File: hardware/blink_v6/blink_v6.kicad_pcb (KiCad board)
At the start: 2 copper layers, 130 x 70 mm, 241 parts, among them J1 RJ45, J12 Conn_01x06, J2 Conn_01x06_Pin, J3 Conn_01x05_Pin, J4 Conn_01x04_Pin, J5 Conn_01x06_Pin, J6 Conn_01x04_Pin, J7 Conn_01x04_Pin, J8 Conn_01x02, J9 Conn_02x10_Odd_Even, Q1 2N7002, Q10 2N7002, Q2 2N7002, Q3 2N7002, Q4 2N7002, Q5 2N7002, Q6 2N7002, Q7 2N7002, Q8 2N7002, Q9 2N7002, U1 ADA4807-1, U10 STM32F405RGTx, U11 AMS1117-3.3, U12 BA50DD0WHFP-TR, U13 M24C02-RMN, U2 SN74LVC1G14DBV, U3 SN74LVC1G14DBV, U4 ADA4807-1, U5 ADA4807-1, U6 TLV3603DCKR, U7 SN74LVC1G14DBV, U8 TLV3603DCKR, U9 L78L05_SOT89, X2 GTXO-14V (2.048MHz), Y1 AOCJY4A-10.000MHZ-SW, Y2 16MHz

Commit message: star clean up of blink board
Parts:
- removed ANT3, ANT4, ANT5, ANT6: U.FL-R-SMT-1, blinky_footprints:U.FL-R-SMT-1
- removed C1, C10, C17, C18, C2, C25, C26, C33, C45, C46, C48, C49: 100nF, Capacitor_SMD:C_0402_1005Metric
- removed C12, C14, C19, C23, C5, C7: 150pF, Capacitor_SMD:C_0603_1608Metric
- removed C13, C20, C8: 330pF, Capacitor_SMD:C_0603_1608Metric
- removed C15, C22, C6: 220pF, Capacitor_SMD:C_0603_1608Metric
- removed C16, C21, C3: 1nF, Capacitor_SMD:C_0603_1608Metric
- removed C24: 100nF, Capacitor_SMD:C_0603_1608Metric
- removed C34: 10uF, Capacitor_Tantalum_SMD:CP_EIA-3216-18_Kemet-A
- removed C42, C44: 33uF, Capacitor_Tantalum_SMD:CP_EIA-3528-21_Kemet-B
- removed J1: RJ45, Connector_RJ:RJ45_Amphenol_RJHSE5380
- removed J2: Conn_01x06_Pin, Connector_PinHeader_2.54mm:PinHeader_1x06_P2.54mm_Vertical
- removed J3: Conn_01x05_Pin, Connector_PinHeader_2.54mm:PinHeader_1x05_P2.54mm_Vertical
- removed JP1: SolderJumper_2_Bridged, Jumper:SolderJumper-2_P1.3mm_Bridged_RoundedPad1.0x1.5mm
- removed L1, L2, L3, L4, L5, L6: 1uF, Inductor_SMD:L_0805_2012Metric
- removed R1, R15, R16: 100R, Resistor_SMD:R_0603_1608Metric
- removed R10, R2, R6: 510R, Resistor_SMD:R_0603_1608Metric
- removed R11, R3, R7: 49R9, Resistor_SMD:R_0603_1608Metric
- removed R12, R13: 1K5, Resistor_SMD:R_0805_2012Metric
- removed R14: 330R, Resistor_SMD:R_0805_2012Metric
- removed R17: 20R, Resistor_SMD:R_0805_2012Metric
- removed R18, R21: 130K, Resistor_SMD:R_0603_1608Metric
- removed R19, R20, R22, R24, R60, R61: 1K0, Resistor_SMD:R_0603_1608Metric
- removed R23: 22K, Resistor_SMD:R_0805_2012Metric
- removed R25: 270R, Resistor_SMD:R_0603_1608Metric
- removed R26: 22R0, Resistor_SMD:R_0603_1608Metric
- removed R8: 270R, Resistor_SMD:R_0805_2012Metric
- removed R9: 2R, Resistor_SMD:R_0805_2012Metric
- removed RV1: 20K, Potentiometer_SMD:Potentiometer_Bourns_3314G_Vertical
- removed TP10, TP11, TP15, TP18, TP19, TP5, TP6, TP7, TP8, TP9: ~, TestPoint:TestPoint_THTPad_D1.5mm_Drill0.7mm
- removed U1, U4, U5: ADA4807-1, Package_TO_SOT_SMD:SOT-23-6
- removed U12: BA50DD0WHFP-TR, blinky_footprints:DPAK172P1054X200-6N
- removed U6, U8: TLV3603DCKR, blinky_footprints:SC70_DCK_TEX
- removed U7: SN74LVC1G14DBV, Package_TO_SOT_SMD:SOT-23-5
- removed U9: L78L05_SOT89, Package_TO_SOT_SMD:SOT-89-3
- removed Y1: AOCJY4A-10.000MHZ-SW, blinky_footprints:XTAL_AOCJY4A-10.000MHZ-SW
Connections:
- net OSC_ADJ renamed /OSC_ADJ
- U10 pad 14: AUX_CLK -> /AUX_CLK
- U10 pad 15: AUX_GPS_PPS -> /AUX_GPS_PPS
- U10 pad 29: GPS_PPS -> /GPS_PPS
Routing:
- net GND: track 1188.4 -> 802.8 mm, vias 59 -> 37
- net +3.3VA: track 229.6 -> 107.2 mm, vias 9 -> 4
- net +5V: track 122.2 -> 0.00 mm, vias 4 -> 0
- net +5VA: track 112.9 -> 0.00 mm, vias 6 -> 0
- net +6V: track 211.6 -> 106.7 mm, vias 7 -> 3
- net /GPS_TX1: track 105.7 -> 1.43 mm, vias 3 -> 0
- net /GPS_RX1: track 98.1 -> 1.16 mm, vias 2 -> 0
- net AUX_CLK: track 77.2 -> 0.00 mm, vias 4 -> 0
- net /GPS_EXT_PPS: track 76.2 -> 0.00 mm, vias 2 -> 0
- net GPS_PPS: track 71.2 -> 0.00 mm, vias 4 -> 0
- net /10Mhz2.5V: track 65.8 -> 0.00 mm, vias 4 -> 0
- net /OCXO_OUT: track 62.9 -> 0.00 mm, vias 1 -> 0
- net /OSC_ADJ: track 107.4 -> 47.2 mm, vias 6 -> 3
- net Net-(J3-Pin_1): track 59.8 -> 0.00 mm, vias 1 -> 0
- net AUX_GPS_PPS: track 59.7 -> 0.00 mm, vias 4 -> 0
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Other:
- board text removed: "5V"
- board text removed: "5VA"
- board text removed: "CH1"
- board text removed: "CH2"
- board text removed: "CH3"
- board text removed: "FrqAdj"
- board text removed: "GPS"
- board text removed: "GpsPps"
- board text removed: "OscIn"
- board text removed: "OscM"

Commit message: moved parts from audio test board into blink board
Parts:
- removed the H5 at (103.3, 99.6)
- added C13: 10uF, Capacitor_SMD:C_0805_2012Metric, F.Cu at (67.3, 100.5)
- added C17: 0.1uF, Capacitor_SMD:C_0805_2012Metric, F.Cu at (67.3, 103.5)
- added C5: 10uF, Capacitor_Tantalum_SMD:CP_EIA-3216-18_Kemet-A, F.Cu at (85.7, 107.3)
- added C6: 0.1uF, Capacitor_SMD:C_0805_2012Metric, F.Cu at (67.3, 88.5)
- added C7: 10uF, Capacitor_SMD:C_0805_2012Metric, F.Cu at (67.3, 91.5)
- added C8: 10uF, Capacitor_SMD:C_0805_2012Metric, F.Cu at (67.3, 94.5)
- added C9: 0.1uF, Capacitor_SMD:C_0805_2012Metric, F.Cu at (67.3, 97.5)
- added H2: M2, MountingHole:MountingHole_2.2mm_M2, F.Cu at (2.48, 2.48)
- added J10: Conn_01x04_Pin, Connector_PinHeader_2.54mm:PinHeader_1x04_P2.54mm_Vertical_SMD_Pin1Left, F.Cu at (70.1, 76.6)
- added J11: KH-BNC50-3511, blinky_footprints:BNC_Amphenol_B6252HB-NPP3G-50_Horizontal-CJ, F.Cu at (31.5, 60.0)
- added J12: Conn_01x04_Pin, Connector_PinHeader_2.54mm:PinHeader_1x04_P2.54mm_Vertical_SMD_Pin1Left, F.Cu at (84.3, 77.5)
- added J13: KH-BNC50-3511, blinky_footprints:BNC_Amphenol_B6252HB-NPP3G-50_Horizontal-CJ, F.Cu at (72.3, 56.8)
- added J2: PJ-320D, blinky_footprints:Jack_3.5mm_PJ320D_Horizontal-CJ, F.Cu at (90.7, 30.5)
- added J3: PJ-320D, blinky_footprints:Jack_3.5mm_PJ320D_Horizontal-CJ, F.Cu at (49.9, 33.7)
- added J4: Conn_01x04_Pin, Connector_PinHeader_2.54mm:PinHeader_1x04_P2.54mm_Vertical_SMD_Pin1Left, F.Cu at (54.4, 78.0)
- added R1: 1K5, Resistor_SMD:R_0805_2012Metric, F.Cu at (71.8, 100.7)
- added R10: 47k, Resistor_SMD:R_0805_2012Metric, F.Cu at (80.6, 100.7)
- added R11: 47k, Resistor_SMD:R_0805_2012Metric, F.Cu at (80.6, 103.7)
- added R13: 560R, Resistor_SMD:R_0805_2012Metric, F.Cu at (80.6, 106.6)
- added R16: 560R, Resistor_SMD:R_0805_2012Metric, F.Cu at (80.6, 109.6)
- added R2: 560R, Resistor_SMD:R_0805_2012Metric, F.Cu at (71.8, 103.7)
- added R3: 47k, Resistor_SMD:R_0805_2012Metric, F.Cu at (71.8, 106.6)
- added R4: 47k, Resistor_SMD:R_0805_2012Metric, F.Cu at (71.8, 109.6)
- added R5: 1K, Resistor_SMD:R_0805_2012Metric, F.Cu at (76.2, 100.7)
- added R6: 10K, Resistor_SMD:R_0805_2012Metric, F.Cu at (76.2, 103.7)
- added R7: 100R, Resistor_SMD:R_0805_2012Metric, F.Cu at (76.2, 106.6)
- added R8: 22K, Resistor_SMD:R_0805_2012Metric, F.Cu at (76.2, 109.6)
- added U2: AD8397, Package_SO:SOIC-8_3.9x4.9mm_P1.27mm, F.Cu at (87.0, 102.5)
- renumbered ANT2 to ANT1, ANT1 to ANT2, C39 to C1, C27 to C10, C29 to C11, C32 to C12, C28 to C14, C36 to C15, C35 to C16, C31 to C18, C40 to C19, C43 to C2, C47 to C20, C38 to C21, C30 to C22, C11 to C23, C9 to C24, C4 to C25, C41 to C3, C37 to C4, D42 to D10, D17 to D11, D18 to D12, D15 to D13, D16 to D14, D12 to D15, D10 to D16, D6 to D17, D43 to D18, D44 to D19, D45 to D20, D19 to D21, D20 to D22, D21 to D23, D22 to D24, D13 to D25, D37 to D26, D38 to D27, D39 to D28, D28 to D29, D34 to D30, D25 to D32, D14 to D33, D46 to D34, D47 to D35, D48 to D36, D29 to D37, D35 to D38, D32 to D39, D8 to D4, D26 to D40, D23 to D41, D11 to D42, D7 to D43, D49 to D44, D50 to D45, D51 to D46, D30 to D47, D36 to D48, D33 to D49, D4 to D5, D27 to D50, D24 to D51, D5 to D6, D9 to D7, D40 to D8, D41 to D9, H2 to H3, H3 to H4, H4 to H5, J8 to J1, J9 to J14, J7 to J5, J5 to J7, J12 to J8, J4 to J9, Q9 to Q1, Q4 to Q10, Q10 to Q2, Q5 to Q3, Q1 to Q4, Q2 to Q5, Q3 to Q8, Q8 to Q9, R58 to R12, R28 to R14, R59 to R15, R54 to R17, R32 to R18, R30 to R19, R62 to R20, R29 to R21, R31 to R22, R5 to R23, R4 to R24, R41 to R25, R33 to R26, R42 to R27, R63 to R28, R64 to R29, R34 to R30, R35 to R31, R43 to R32, R36 to R33, R44 to R34, R50 to R35, R49 to R36, R55 to R37, R56 to R38, R57 to R39, R52 to R40, R53 to R41, R51 to R42, R45 to R43, R37 to R44, R46 to R45, R38 to R46, R39 to R48, R48 to R49, R40 to R50, R27 to R9, TP17 to TP1, TP16 to TP2, TP12 to TP3, TP13 to TP4, TP14 to TP5, TP1 to TP6, TP4 to TP7, TP2 to TP8, TP3 to TP9, U11 to U1, U13 to U3, U10 to U4, U2 to U5, U3 to U6, X2 to X1, Y2 to Y1

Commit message: updating board shape
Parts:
- removed R1: 1K5, Resistor_SMD:R_0805_2012Metric
- J12, J4: value Conn_01x04_Pin -> KH-BNC50-3511; footprint Connector_PinHeader_2.54mm:PinHeader_1x04_P2.54mm_Vertical_SMD_Pin1Left -> blinky_footprints:BNC_Amphenol_B6252HB-NPP3G-50_Horizontal-CJ
- moved J4 212.0 mm to (266.4, 71.6), turned to 90 degrees
- moved J3 95.0 mm to (118.0, 100.0)
- moved J11 90.4 mm to (121.5, 52.0), turned to 90 degrees
- moved H2 77.0 mm to (63.8, 49.0)
- moved J13 77.0 mm to (121.5, 116.0), turned to 90 degrees
- moved C5 56.6 mm to (140.9, 94.7), turned to 90 degrees
- moved J2 46.4 mm to (118.0, 68.0)
- moved U2 45.6 mm to (132.5, 99.7), turned to 90 degrees
- moved H4 41.1 mm to (118.9, 127.4)
- moved ANT2 40.2 mm to (136.0, 52.0)
- moved C23 40.2 mm to (148.3, 52.7)
- moved C25 40.2 mm to (140.9, 53.4)
- moved R23 40.2 mm to (139.6, 59.6)
- moved TP6 40.2 mm to (132.6, 50.6)
- moved TP8 40.2 mm to (132.5, 53.4)
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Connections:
- J12 pad 1: GND -> unconnected-(J12-In-Pad1)
- J12 pad 2: Net-(J12-Pin_2) -> unconnected-(J12-Ext-Pad2)
- J4 pad 1: GND -> unconnected-(J4-In-Pad1)
- J4 pad 2: /Left -> unconnected-(J4-Ext-Pad2)
- R2 pad 2: Net-(J12-Pin_2) -> Net-(U2B--)
- U2 pad 6: Net-(J12-Pin_2) -> Net-(U2B--)
- U2 pad 7: Net-(J12-Pin_2) -> Net-(U2B--)
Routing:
- net GND: track 802.8 -> 749.6 mm
- net SYNC_IN: track 88.7 -> 47.6 mm
- net SYNC_OUT: track 125.6 -> 84.6 mm
- net SYNC_IN2: track 86.2 -> 45.6 mm
- net +3.3V: track 395.2 -> 383.9 mm
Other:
- board size 130 x 70 mm -> 119 x 92 mm

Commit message: start re-layout of board
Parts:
- removed ANT1, ANT2: U.FL-R-SMT-1, blinky_footprints:U.FL-R-SMT-1
- removed D1, D16, D17, D4, D42, D43, D5, D6, D7: LED-RED, LED_SMD:LED_0603_1608Metric
- removed D10, D11, D12, D13, D14, D15, D18, D19, D2, D20, D21, D22, D23, D24, D25, D26, D27, D28, D29, D30, D31, D32, D33, D34, D35, D36, D37, D38, D39, D40, D41, D44, D45, D46, D47, D48, D49, D50, D51, D8, D9: LED-G, LED_SMD:LED_0603_1608Metric
- removed D3: LED-Y, LED_SMD:LED_0603_1608Metric
- removed H2: M2, MountingHole:MountingHole_2.2mm_M2
- removed Q1, Q10, Q2, Q3, Q4, Q5, Q6, Q7, Q8, Q9: 2N7002, Package_TO_SOT_SMD:SOT-23
- removed R19, R21, R22, R27, R30, R33, R34, R45, R46, R49, R50: 100R, Resistor_SMD:R_0603_1608Metric
- removed R25, R26, R31, R32, R43, R44, R47, R48: 4K7, Resistor_SMD:R_0603_1608Metric
- removed R35, R36, R37, R38, R39, R40, R41, R42: 82R, Resistor_SMD:R_0603_1608Metric
- removed TP1, TP2, TP3, TP4, TP5, TP6, TP7, TP8, TP9: ~, TestPoint:TestPoint_THTPad_D1.5mm_Drill0.7mm
- J14: value Conn_02x10_Odd_Even -> Conn_02x16_Odd_Even; footprint Connector_PinHeader_2.54mm:PinHeader_2x10_P2.54mm_Vertical -> Connector_PinHeader_2.54mm:PinHeader_2x16_P2.54mm_Vertical
- moved J9 109.2 mm to (78.0, 63.8), turned to 0 degrees
- moved X1 96.1 mm to (131.0, 103.8), turned to 0 degrees
- moved R4 94.3 mm to (143.5, 82.2), turned to 180 degrees
- moved R3 82.2 mm to (139.4, 82.2), turned to 180 degrees
- moved C9 78.3 mm to (143.5, 79.2), turned to 180 degrees
- moved C6 76.6 mm to (141.9, 71.2), turned to -90 degrees
- moved C17 74.8 mm to (130.3, 63.2), turned to -90 degrees
- moved J7 69.2 mm to (186.7, 121.3)
- moved J10 68.3 mm to (137.5, 87.8), turned to 90 degrees
- moved R13 67.9 mm to (129.3, 59.4)
- moved R7 67.5 mm to (130.7, 66.9)
- moved C8 67.2 mm to (132.9, 79.9)
- moved C10 65.7 mm to (155.9, 118.1), turned to -90 degrees
- moved C7 63.4 mm to (125.7, 66.9)
- moved R11 62.4 mm to (128.1, 63.2), turned to -90 degrees
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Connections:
- C25 pad 2: Net-(ANT2-PadSIG) -> Net-(J12-In)
- C5 pad 1: +3.3V -> +3.3VA
- C6 pad 2: +3.3V -> +3.3VA
- J12 pad 1: unconnected-(J12-In-Pad1) -> Net-(J12-In)
- J12 pad 2: unconnected-(J12-Ext-Pad2) -> GND
- J14 pad 1: GND -> +3.3V
- J14 pad 10: /LEDH -> /COL2
- J14 pad 11: /LEDG -> /LEDF
- J14 pad 12: /LEDF -> /LEDG
- J14 pad 13: /ROW4 -> /ROW3
- J14 pad 14: /ROW3 -> /ROW4
- J14 pad 15: /ROW2 -> /ROW1
- J14 pad 16: /ROW1 -> /ROW2
- J14 pad 17: /LEDE -> /LEDD
- J14 pad 18: /LEDD -> /LEDE
- J14 pad 19: /LEDC -> /LEDB
- J14 pad 2: +3.3V -> +6V
- J14 pad 20: /LEDB -> /LEDC
- J14 pad 3: /ROW5 -> GND
- J14 pad 4: /LEDA -> GND
- J14 pad 5: /COL3 -> /COL5
- J14 pad 6: /COL5 -> /COL3
- J14 pad 7: /COL4 -> /COL1
- J14 pad 8: /COL1 -> /COL4
- J14 pad 9: /COL2 -> /LEDH
- J4 pad 1: unconnected-(J4-In-Pad1) -> Net-(J4-In)
- J4 pad 2: unconnected-(J4-Ext-Pad2) -> GND
- J7 pad 2: SYNC_OUT -> /AUX_SYNC_MON
- R10 pad 2: +3.3V -> +3.3VA
- R23 pad 1: Net-(ANT1-PadSIG) -> Net-(J4-In)
- R24 pad 2: Net-(ANT2-PadSIG) -> Net-(J12-In)
- R3 pad 2: +3.3V -> +3.3VA
- U2 pad 8: +3.3V -> +3.3VA
- U6 pad 2: Net-(ANT1-PadSIG) -> Net-(J4-In)
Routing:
- net GND: track 749.6 -> 451.8 mm, vias 37 -> 2
- net +3.3V: track 383.9 -> 131.6 mm, vias 14 -> 4
- net /COL3: track 96.3 -> 7.28 mm, vias 10 -> 0
- net /COL1: track 94.0 -> 7.16 mm, vias 10 -> 0
- net +6V: track 106.7 -> 21.0 mm, vias 3 -> 0
- net /COL5: track 91.8 -> 7.03 mm, vias 10 -> 0
- net /COL2: track 90.3 -> 7.39 mm, vias 10 -> 0
- net /COL4: track 89.4 -> 6.70 mm, vias 10 -> 0
- net +3.3VA: track 107.2 -> 25.4 mm, vias 4 -> 0
- net SYNC_OUT: track 84.6 -> 18.5 mm, vias 5 -> 1
- net /LEDB: track 98.3 -> 34.6 mm, vias 1 -> 0
- net /LEDD: track 90.8 -> 31.6 mm, vias 1 -> 0
- net /AUD_OUT: track 73.5 -> 16.3 mm, vias 2 -> 1
- net /LEDC: track 89.7 -> 32.9 mm, vias 1 -> 0
- net /LB: track 56.4 -> 0.00 mm, vias 2 -> 0
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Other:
- board text added: "Blink Rev 6.0 Cullen Jennings 2023"
- board text added: "RESET"
- board text removed: "6V Power"
- board text removed: "Blinky Rev6.0 Cullen Jennings"
- board text removed: "Boot0"
- board text removed: "NRst"
- board text removed: "SIn"
- board text removed: "SOut"
- board text removed: "SWD"

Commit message: part placement
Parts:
- removed J9: Conn_01x04_Pin, Connector_PinHeader_2.54mm:PinHeader_1x04_P2.54mm_Vertical
- added C26: 10uF, Capacitor_SMD:C_0805_2012Metric, F.Cu at (148.4, 70.0)
- added R1: 560R, Resistor_SMD:R_0805_2012Metric, F.Cu at (151.3, 70.0)
- added R19: 560R, Resistor_SMD:R_0805_2012Metric, F.Cu at (154.3, 70.0)
- J10: footprint Connector_PinHeader_2.54mm:PinHeader_1x04_P2.54mm_Vertical_SMD_Pin1Left -> Connector_PinHeader_2.54mm:PinHeader_1x04_P2.54mm_Vertical
- moved R8 77.5 mm to (147.7, 60.5), turned to 180 degrees
- moved C13 67.4 mm to (129.7, 56.0), turned to 90 degrees
- moved R6 60.6 mm to (130.2, 59.6)
- moved R2 55.8 mm to (130.7, 76.1), turned to -90 degrees
- moved R5 52.3 mm to (134.8, 82.7), turned to 180 degrees
- moved R16 51.7 mm to (137.0, 86.7), turned to 90 degrees
- moved J10 35.0 mm to (150.6, 55.3)
- moved R7 24.2 mm to (154.1, 60.7)
- moved R13 10.1 mm to (129.4, 49.3), turned to 90 degrees
- moved J6 9.95 mm to (158.8, 49.2), turned to -90 degrees
- moved C7 6.99 mm to (130.6, 71.9), turned to 90 degrees
- moved C5 3.43 mm to (142.8, 73.7)
- moved U2 3.43 mm to (135.6, 72.6)
- moved C6 3.43 mm to (140.2, 74.2)
- moved R11 1.47 mm to (129.3, 64.0)
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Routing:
- net GND: track 451.8 -> 436.1 mm
- net /AUD_IN: track 18.5 -> 16.9 mm
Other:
- board text removed: "I2C"
- board text removed: "RX/TX"

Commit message: update routing
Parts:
- moved C6 9.63 mm to (132.7, 68.2)
- moved C5 9.63 mm to (135.3, 67.7)
- moved J10 4.24 mm to (146.8, 57.1)
- moved R3 3.87 mm to (139.3, 86.1), turned to -90 degrees
- moved U2 3.87 mm to (139.3, 73.6), turned to 90 degrees
- moved R28 3.70 mm to (137.4, 60.6), turned to 0 degrees
- moved R15 3.68 mm to (170.6, 109.0), turned to -90 degrees
- moved R12 2.30 mm to (165.3, 113.7), turned to 180 degrees
- moved C9 2.20 mm to (141.3, 79.8)
- moved R4 2.17 mm to (141.3, 82.0)
- moved C20 2.09 mm to (169.6, 106.5)
- moved J5 1.89 mm to (174.6, 108.6)
- moved C13 1.77 mm to (129.0, 54.4), turned to -90 degrees
- moved R9 1.69 mm to (155.7, 115.2), turned to 0 degrees
- moved R19 1.55 mm to (152.8, 69.6)
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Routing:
- net Net-(J4-In): track 7.40 -> 88.5 mm, vias 0 -> 2
- net +3.3V: track 131.6 -> 56.0 mm, vias 4 -> 1
- net /Right: track 0.00 -> 51.2 mm
- net Net-(J10-Pin_2): track 0.00 -> 47.6 mm, vias 0 -> 4
- net /Mic: track 0.00 -> 45.3 mm, vias 0 -> 2
- net /Left: track 0.00 -> 44.9 mm, vias 0 -> 2
- net Net-(J12-In): track 6.83 -> 51.1 mm, vias 0 -> 3
- net SYNC_OUT: track 18.5 -> 62.4 mm, vias 1 -> 2
- net /AUX_SYNC_MON: track 2.73 -> 46.6 mm, vias 0 -> 2
- net /SWDCLK: track 7.03 -> 47.7 mm, vias 1 -> 4
- net Net-(J13-In): track 0.00 -> 39.9 mm
- net Net-(J10-Pin_3): track 0.00 -> 38.8 mm, vias 0 -> 2
- net /DB3: track 21.2 -> 59.3 mm, vias 1 -> 2
- net /DB2: track 21.2 -> 57.8 mm, vias 1 -> 2
- net /DB1: track 19.4 -> 55.2 mm, vias 1 -> 2
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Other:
- board text removed: "3.3V"
- board text removed: "3.3VA"

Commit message: signal routing done
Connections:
- J14 pad 10: /COL2 -> /ROW1
- J14 pad 11: /LEDF -> /ROW4
- J14 pad 12: /LEDG -> /ROW3
- J14 pad 13: /ROW3 -> /LEDG
- J14 pad 14: /ROW4 -> /LEDF
- J14 pad 15: /ROW1 -> /LEDA
- J14 pad 16: /ROW2 -> /LEDH
- J14 pad 17: /LEDD -> /LEDM1
- J14 pad 18: /LEDE -> /LEDM3
- J14 pad 19: /LEDB -> /ROW7
- J14 pad 20: /LEDC -> /ROW6
- J14 pad 21: /ROW7 -> /BOOT1
- J14 pad 22: /ROW6 -> /ROW8
- J14 pad 23: /LEDM1 -> /COL5
- J14 pad 24: /ROW8 -> /COL4
- J14 pad 25: /LEDM3 -> /ROW5
- J14 pad 26: /LEDM2 -> /COL3
- J14 pad 27: /LEDA -> /COL1
- J14 pad 28: /ROW5 -> /COL2
- J14 pad 29: unconnected-(J14-Pin_29-Pad29) -> /AUX_CLK
- J14 pad 30: unconnected-(J14-Pin_30-Pad30) -> /LEDM2
- J14 pad 31: unconnected-(J14-Pin_31-Pad31) -> /AUX_GPS_PPS
- J14 pad 32: unconnected-(J14-Pin_32-Pad32) -> /AUX_SYNC_MON
- J14 pad 5: /COL5 -> /LEDC
- J14 pad 6: /COL3 -> /LEDB
- J14 pad 7: /COL1 -> /LEDE
- J14 pad 8: /COL4 -> /LEDD
- J14 pad 9: /LEDH -> /ROW2
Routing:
- net GND: track 416.9 -> 723.7 mm, vias 1 -> 25
- net /AUX_CLK: track 0.00 -> 26.6 mm, vias 0 -> 2
- net /AUX_GPS_PPS: track 0.00 -> 26.0 mm, vias 0 -> 2
- net /USB_RX: track 47.1 -> 72.5 mm, vias 3 -> 4
- net /ROW1: track 23.9 -> 48.9 mm
- net /ROW2: track 23.2 -> 45.1 mm
- net /ROW3: track 26.0 -> 47.8 mm
- net /LEDE: track 25.4 -> 47.1 mm
- net /LEDF: track 24.7 -> 45.3 mm
- net /COL2: track 7.39 -> 26.9 mm
- net /ROW4: track 25.1 -> 44.1 mm
- net /ROW6: track 23.0 -> 41.5 mm
- net /LEDM3: track 26.6 -> 45.0 mm
- net /LEDD: track 31.6 -> 49.9 mm
- net /LEDH: track 25.2 -> 43.4 mm
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
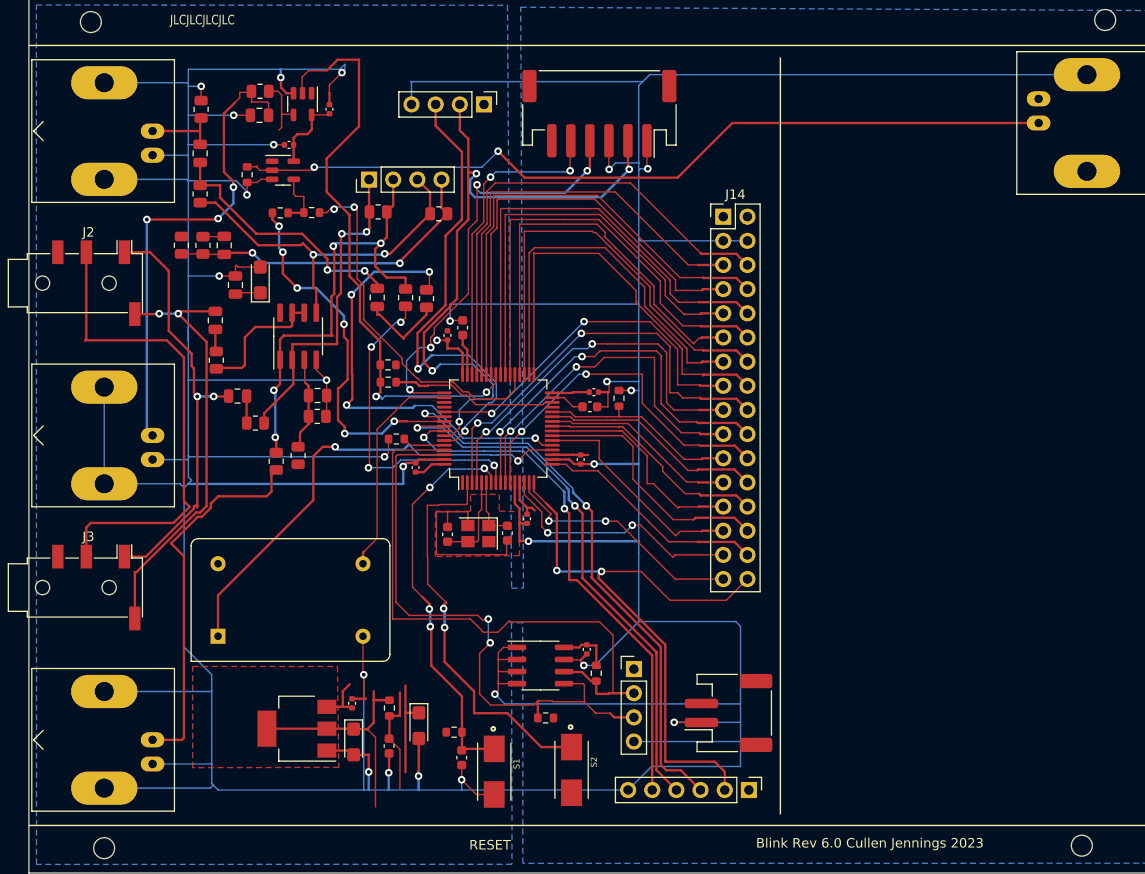
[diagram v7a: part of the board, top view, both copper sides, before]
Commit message: basic routing connectivity
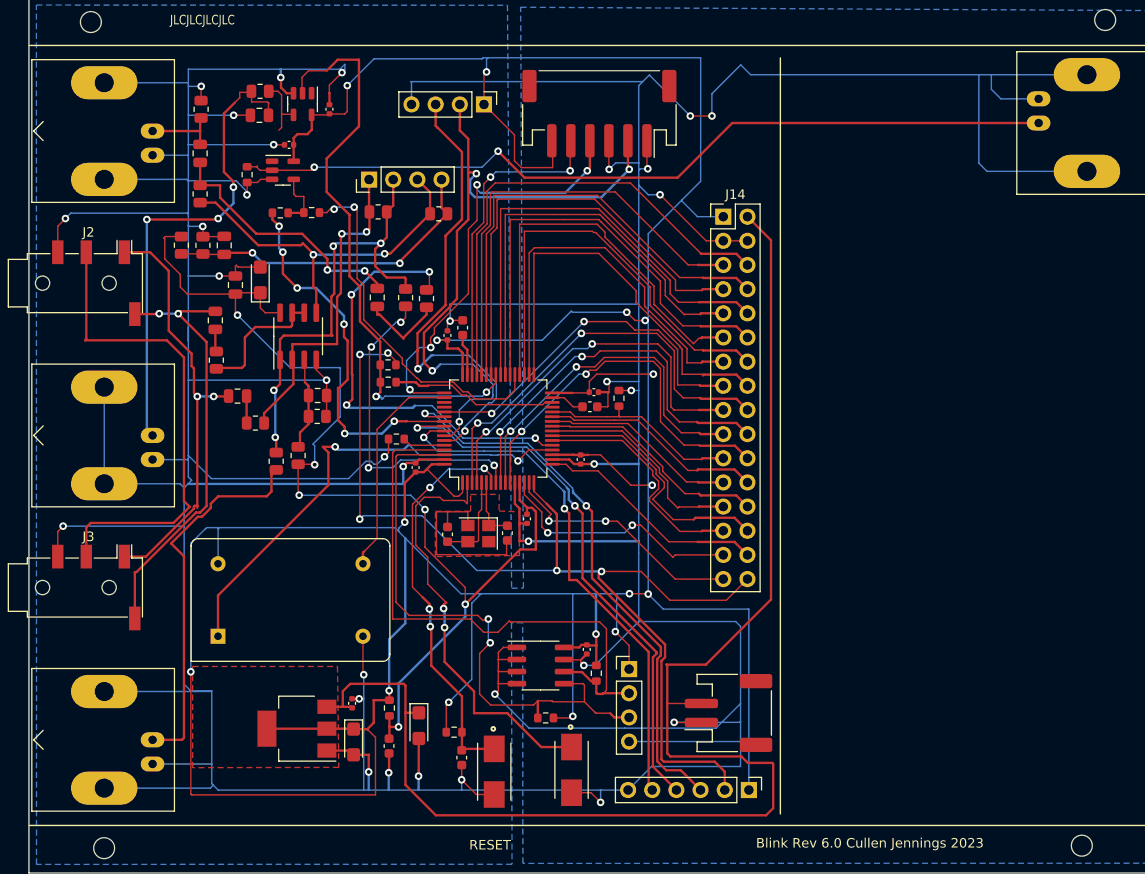
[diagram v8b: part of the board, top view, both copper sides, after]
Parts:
- moved J5 0.50 mm to (174.1, 108.6)
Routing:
- net +3.3V: track 56.0 -> 429.1 mm, vias 1 -> 16
- net +6V: track 15.9 -> 147.8 mm
- net +3.3VA: track 19.1 -> 115.7 mm, vias 0 -> 6
- net GND: track 723.7 -> 804.4 mm, vias 25 -> 33
- net /AUX_SYNC_MON: track 64.1 -> 109.7 mm, vias 2 -> 5
- net /ROW8: track 37.6 -> 40.2 mm
- net /BTN1: track 42.5 -> 44.7 mm
- net /COL1: track 23.5 -> 24.8 mm
- net /COL2: track 26.9 -> 27.9 mm
- net /LEDM3: track 45.0 -> 44.5 mm
